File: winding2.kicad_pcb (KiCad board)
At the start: 2 copper layers, 115.9 x 78.6 mm, 23 parts, among them J1 Screw_Terminal_2_P5.00mm, J2 Limit Switches, J3 Screw Stepper, J4 Main Stepper, J5 RPM & ESC, J6 5V input, J7 ESC XT60, J8 ARDUINO PROG., SW1 RotaryEncoder_Switch, U1 TMC2209_SILENTSTEPSTICK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

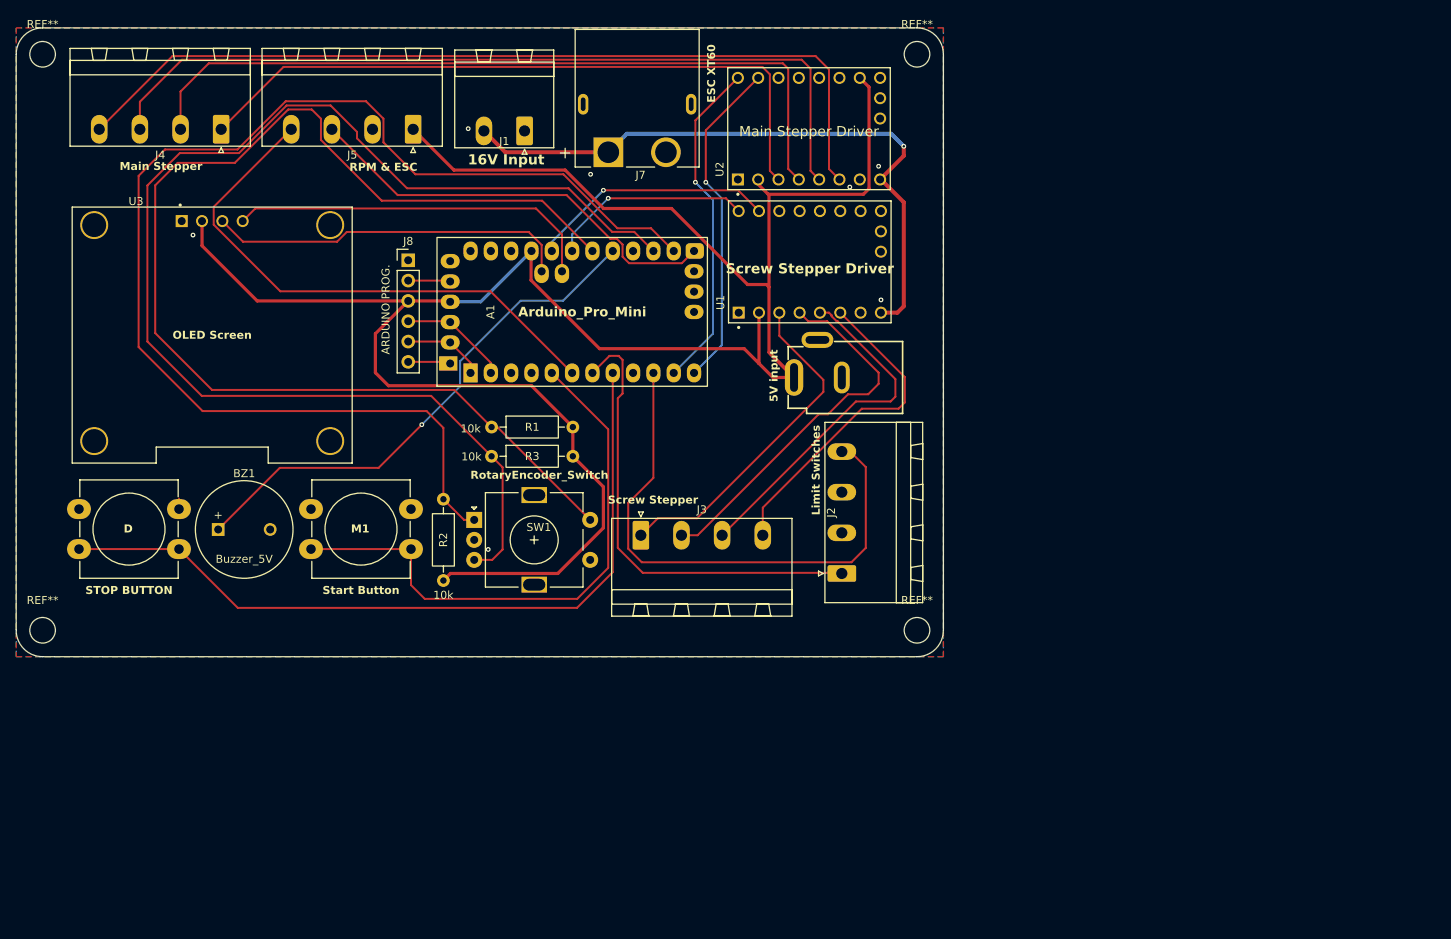
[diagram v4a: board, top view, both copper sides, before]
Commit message: mounting holes silkscreen label added
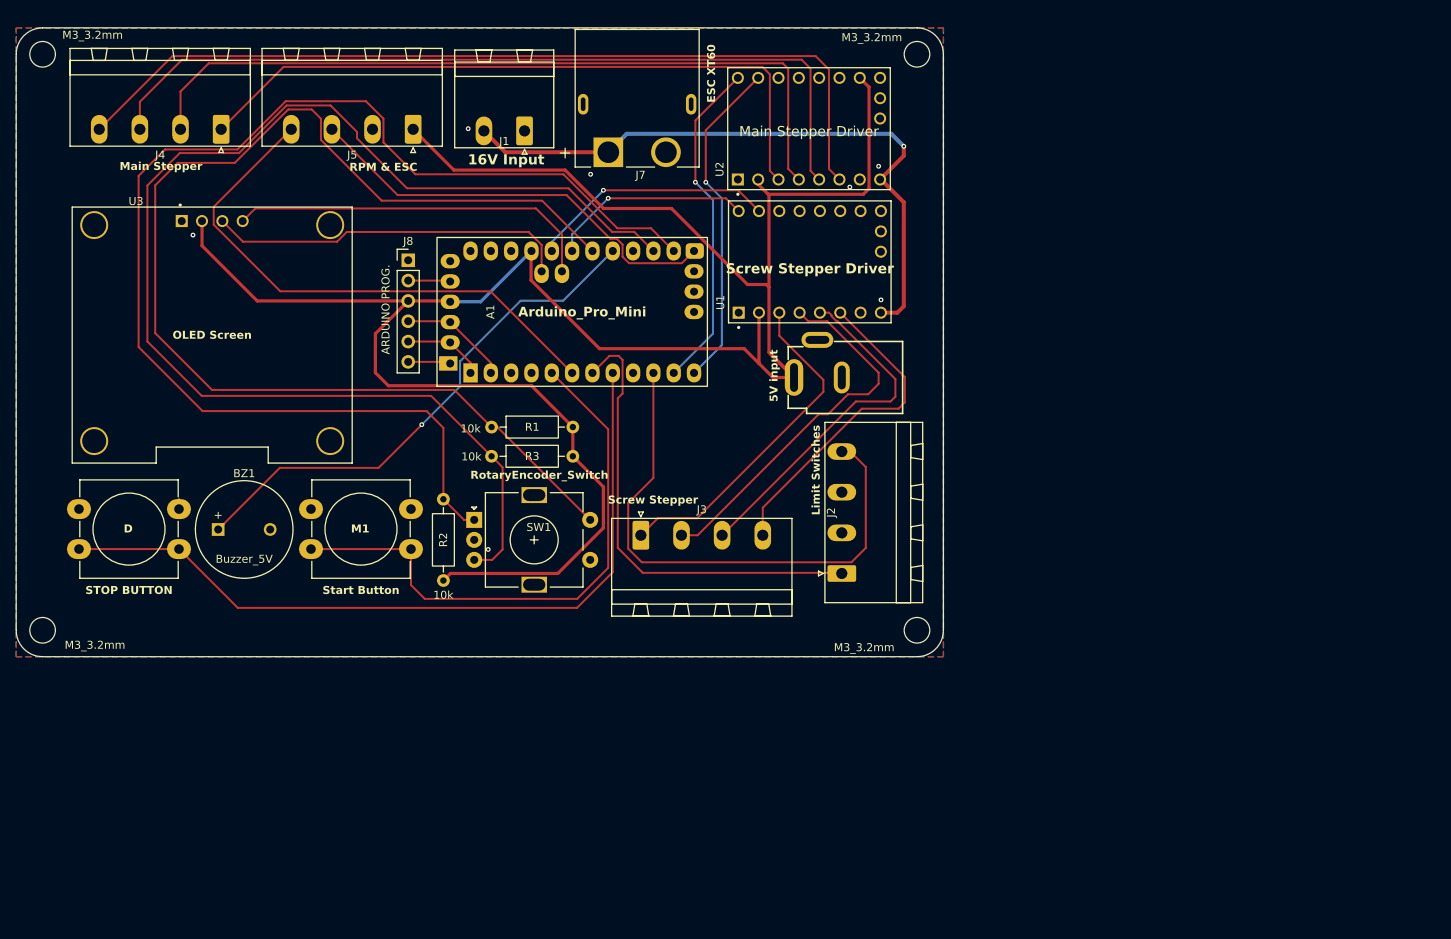
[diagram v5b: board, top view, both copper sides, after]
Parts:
- renumbered REF** to M3_3.2mm
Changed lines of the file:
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@@
 		(descr "Mounting Hole 3.2mm, M3, no annular, generated by kicad-footprint-generator mountinghole.py")
 		(tags "mountinghole M3 DIN965")
-		(property "Reference" "REF**"
-			(at 0 -3.75 0)
+		(property "Reference" "M3_3.2mm"
+			(at -6.6 2.15 0)
 			(layer "F.SilkS")
 			(effects
@@
 		(descr "Mounting Hole 3.2mm, M3, no annular, generated by kicad-footprint-generator mountinghole.py")
 		(tags "mountinghole M3 DIN965")
-		(property "Reference" "REF**"
-			(at 0 -3.75 0)
+		(property "Reference" "M3_3.2mm"
+			(at 6.55 1.85 0)
 			(layer "F.SilkS")
 			(effects
@@
 		(descr "Mounting Hole 3.2mm, M3, no annular, generated by kicad-footprint-generator mountinghole.py")
 		(tags "mountinghole M3 DIN965")
-		(property "Reference" "REF**"
-			(at 0 -3.75 0)
+		(property "Reference" "M3_3.2mm"
+			(at 6.25 -2.4 0)
 			(layer "F.SilkS")
 			(effects
@@
 		(descr "Mounting Hole 3.2mm, M3, no annular, generated by kicad-footprint-generator mountinghole.py")
 		(tags "mountinghole M3 DIN965")
-		(property "Reference" "REF**"
-			(at 0 -3.75 0)
-			(layer "F.SilkS")
-			(effects
+		(property "Reference" "M3_3.2mm"
+			(at -5.65 -2.1 0)
+			(layer "F.SilkS")
+			(effects
